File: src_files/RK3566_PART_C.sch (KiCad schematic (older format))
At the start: 1 part

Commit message: littleupdate
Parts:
- U1: renamed from U?; footprint (none) -> greencharge-footprints:BGA828C65P31X31_2100X2100X161N
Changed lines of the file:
@@
 $Descr A3 16535 11693
 encoding utf-8
-Sheet 8 11
+Sheet 10 11
 Title ""
 Date ""
@@
 P 7300 650
 AR Path="/61C7A3C9" Ref="U?"  Part="4"
-AR Path="/61C73AB6/61C7A3C9" Ref="U?"  Part="4"
-F 0 "U?" H 7325 315 50  0000 C CNN
+AR Path="/61C73AB6/61C7A3C9" Ref="U1"  Part="4"
+F 0 "U1" H 7325 315 50  0000 C CNN
 F 1 "RK3566" H 7325 224 50  0000 C CNN
-F 2 "" H 6750 550 50  0001 C CNN
+F 2 "greencharge-footprints:BGA828C65P31X31_2100X2100X161N" H 6750 550 50  0001 C CNN
 F 3 "" H 6750 550 50  0001 C CNN
 	4    7300 650

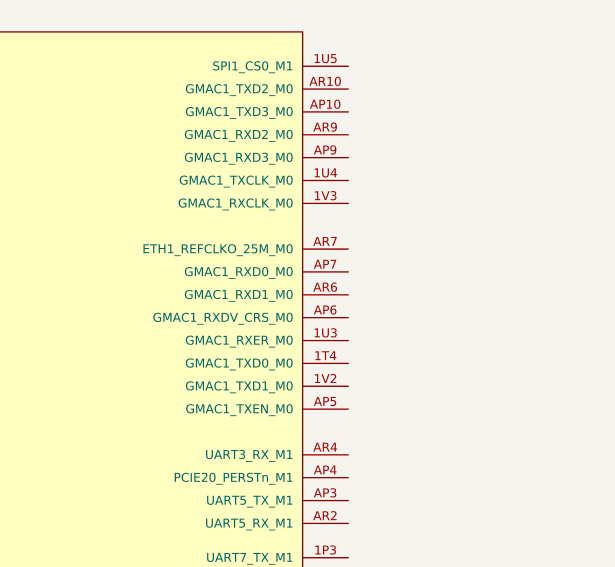
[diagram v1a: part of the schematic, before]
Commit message: gps add
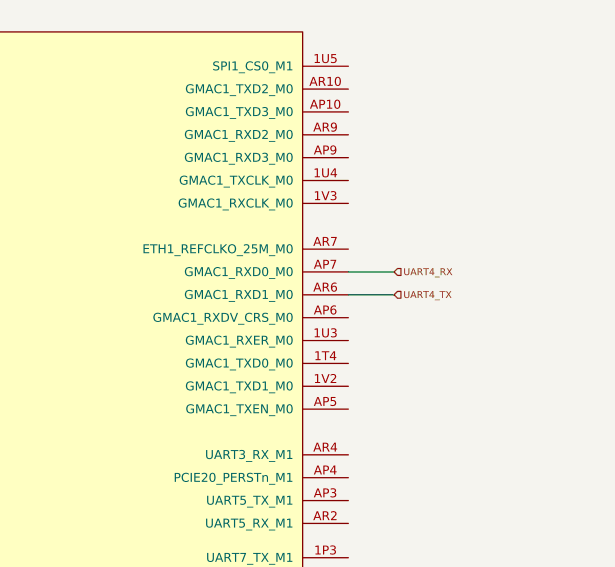
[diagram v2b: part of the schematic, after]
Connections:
- net UART4_RX: now reaches U1.AP7 (GMAC1_RXD0_M0)
- net UART4_TX: now reaches U1.AR6 (GMAC1_RXD1_M0)
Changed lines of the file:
@@
 Wire Wire Line
 	9475 5450 9350 5450
+Text HLabel 9550 2200 2    30   Input ~ 0
+UART4_RX
+Text HLabel 9550 2300 2    30   Input ~ 0
+UART4_TX
+Wire Wire Line
+	9550 2300 9350 2300
+Wire Wire Line
+	9550 2200 9350 2200
 $EndSCHEMATC

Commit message: added 3 screens
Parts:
- added C? (x12): 100nF, symbol Device:C_Small
- added C? (x5): 1uF, symbol Device:C_Small
- added C? (x4): 10uF, symbol Device:C_Small
- added J? (x2): 3-1734592-0, greencharge-footprints:TE_3-1734592-0, symbol 3-1734592-0:3-1734592-0
- added J?: 2001-1-2-21-00-BK, digikey-footprints:HDMI_Mini_Female_2001-1-2-21-00-BK, symbol dk_USB-DVI-HDMI-Connectors:2001-1-2-21-00-BK
- added R? (x4): 1R_1%, symbol Device:R_US
- added TP?: LVDS_TX0_AVDD_0V9, symbol Connector:TestPoint
- added TP?: LVDS_TX0_AVDD_1V8, symbol Connector:TestPoint
- added TP?: LVDS_TX1_AVDD_0V9, symbol Connector:TestPoint
- added TP?: LVDS_TX1_AVDD_1V8, symbol Connector:TestPoint
- added U? (x3): ESD5304D-TP, greencharge-footprints:ESD5304D-TP, symbol GCL_Integrated-Circuits:ESD5304D-TP
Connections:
- net 1N10: now reaches U1.1N10 (MIPI_DSI_TX1_AVDD_0V9)
- net 1N10: now also C?.1, R?.1, TP?.1
- net 1P11: now reaches U1.1P11 (MIPI_DSI_TX0/LVDS_TX0_AVDD_0V9)
- net 1P11: now also C?.1, R?.1, TP?.1
- net 1P12: now reaches U1.1P12 (MIPI_DSI_TX0/LVDS_TX0_AVDD_1V8)
- net 1P12: now also C?.1, R?.1, TP?.1
- net 1R10: now reaches U1.1R10 (IPI_DSI_TX1_AVDD_1V8)
- net 1R10: now also C?.1, R?.1, TP?.1
- net MIPI_DSI_TX1_CLKN-: now reaches U1.1U11 (MIPI_DSI_TX1_CLKn)
- net MIPI_DSI_TX1_CLKN-: now also J?.23
- net MIPI_DSI_TX1_CLKP+: now reaches U1.1V11 (MIPI_DSI_TX1_CLKp)
- net MIPI_DSI_TX1_CLKP+: now also J?.22
- net MIPI_DSI_TX0_CLKN-: now reaches U1.1V15 (MIPI_DSI_TX0_CLKn/LVDS_TX0_CLKn)
- net MIPI_DSI_TX0_CLKN-: now also J?.23
- net MIPI_DSI_TX0_CLKP+: now reaches U1.1V16 (MIPI_DSI_TX0_CLKp/LVDS_TX0_CLKp)
- net MIPI_DSI_TX0_CLKP+: now also J?.22
- net LCD_BL_PWM11_DISPLAY_ONE: now reaches U1.1V2 (GMAC1_TXD1_M0)
- net LCD_BL_PWM11_DISPLAY_ONE: now also J?.12
- net MIPI_DSI_TX1_D3N-: now reaches U1.AP20 (MIPI_DSI_TX1_D3n)
- net MIPI_DSI_TX1_D3N-: now also J?.29
- net MIPI_DSI_TX1_D2P+: now reaches U1.AP21 (MIPI_DSI_TX1_D2p)
- net MIPI_DSI_TX1_D2P+: now also J?.25
- net MIPI_DSI_TX1_D1N-: now reaches U1.AP23 (MIPI_DSI_TX1_D1n)
- net MIPI_DSI_TX1_D1N-: now also J?.20
- net MIPI_DSI_TX1_D0P+: now reaches U1.AP24 (MIPI_DSI_TX1_D0p)
- net MIPI_DSI_TX1_D0P+: now also J?.16
- net MIPI_DSI_TX0_D3N-: now reaches U1.AP26 (MIPI_DSI_TX0_D3n/LVDS_TX0_D3n)
- net MIPI_DSI_TX0_D3N-: now also J?.29
- net MIPI_DSI_TX0_D2P+: now reaches U1.AP27 (MIPI_DSI_TX0_D2p/LVDS_TX0_D2p)
- net MIPI_DSI_TX0_D2P+: now also J?.25
- net MIPI_DSI_TX0_D1N-: now reaches U1.AP29 (MIPI_DSI_TX0_D1n/LVDS_TX0_D1n)
- net MIPI_DSI_TX0_D1N-: now also J?.20
- net MIPI_DSI_TX0_D0P+: now reaches U1.AP30 (MIPI_DSI_TX0_D0p)
- net MIPI_DSI_TX0_D0P+: now also J?.16
- net HDMI_TX0N_PORT-: now reaches U1.AP33 (HDMI_TX_D0p)
- net HDMI_TX0N_PORT-: now also J?.9, U?.4
- net HDMI_TX1N_PORT-: now reaches U1.AP35 (HDMI_TX_D1n)
- net HDMI_TX1N_PORT-: now also J?.6, U?.1
- net HDMI_TX2P_PORT+: now reaches U1.AP36 (HDMI_TX_D2p)
- net HDMI_TX2P_PORT+: now also J?.1, U?.4
- net MIPI_DSI_TX1_D3P+: now reaches U1.AR20 (MIPI_DSI_TX1_D3p)
- net MIPI_DSI_TX1_D3P+: now also J?.28
- net MIPI_DSI_TX1_D2N-: now reaches U1.AR21 (MIPI_DSI_TX1_D2n)
- net MIPI_DSI_TX1_D2N-: now also J?.26
- net MIPI_DSI_TX1_D1P+: now reaches U1.AR23 (MIPI_DSI_TX1_D1p)
- net MIPI_DSI_TX1_D1P+: now also J?.19
- net MIPI_DSI_TX1_D0N-: now reaches U1.AR24 (MIPI_DSI_TX1_D0n)
- net MIPI_DSI_TX1_D0N-: now also J?.17
- net MIPI_DSI_TX0_D3P+: now reaches U1.AR26 (MIPI_DSI_TX0_D3p/LVDS_TX0_D3p)
- net MIPI_DSI_TX0_D3P+: now also J?.28
- net MIPI_DSI_TX0_D2N-: now reaches U1.AR27 (MIPI_DSI_TX0_D2n/LVDS_TX0_D2n)
- net MIPI_DSI_TX0_D2N-: now also J?.26
- net MIPI_DSI_TX0_D1P+: now reaches U1.AR29 (MIPI_DSI_TX0_D1p/LVDS_TX0_D1p)
- net MIPI_DSI_TX0_D1P+: now also J?.19
- net MIPI_DSI_TX0_D0N-: now reaches U1.AR30 (MIPI_DSI_TX0_D0n/LVDS_TX0_D0n)
- net MIPI_DSI_TX0_D0N-: now also J?.17
- net HDMI_TXCLKP_PORT+: now reaches U1.AR33 (HDMI_TX_D0n)
- net HDMI_TXCLKP_PORT+: now also J?.10, U?.3
- net HDMI_TX1P_PORT+: now reaches U1.AR35 (HDMI_TX_D1p)
- net HDMI_TX1P_PORT+: now also J?.4, U?.2
- net HDMI_TX2N_PORT-: now reaches U1.AR36 (HDMI_TX_D2n)
- net HDMI_TX2N_PORT-: now also J?.3, U?.3
- new net +5V: C?.1, C?.1, C?.1, C?.1, C?.1, C?.1, C?.1, C?.1, J?.1, J?.1, J?.2, J?.2, J?.3, J?.3
- new net BL_EN_GPIO0_C0: J?.11
- new net BL_EN_GPIO0_C0_DISPLAY_ONE: J?.11
- new net GND: C?.2, C?.2, C?.2, C?.2, C?.2, C?.2, C?.2, C?.2, C?.2, C?.2, C?.2, C?.2, C?.2, C?.2, C?.2, C?.2, C?.2, C?.2, C?.2, C?.2, C?.2, J?.11, J?.15, J?.15, J?.17, J?.18, J?.18, J?.2, J?.21, J?.21, J?.24, J?.24, J?.27, J?.27, J?.30, J?.30, J?.4, J?.4, J?.5, J?.8, J?.S1 (SHIELD), J?.S1 (SHIELD), J?.S2 (SHIELD), J?.S2 (SHIELD), U?.5 (GND), U?.5 (GND), U?.5 (GND)
- new net GNDPWR: J?.SH
- new net GPIO0_A0_DISPLAY_ONE: J?.5
- new net GPIO0_A0_DISPLAY_ZERO: J?.5
- new net HDMI_TX0P_PORT+: J?.7
- new net HDMI_TXCLKN_PORT-: J?.12, U?.2
- new net HDMI_TXDDC_SCL_PORT: J?.15, U?.4
- new net HDMI_TXDDC_SDA_PORT: J?.16, U?.3
- new net HDMI_TX_CEC_PORT: J?.13, U?.1
- new net HDMI_TX_HPD_PORT: J?.19, U?.2
- new net I2C2_SCL_M0_TP: J?.8, J?.8
- new net I2C2_SDA_M0_TP: J?.7, J?.7
- new net LCD_1_EN_GPIO0_C7: J?.9
- new net LCD_BL_PWM4: J?.12
- new net LCD_EN_GPIO0_C7: J?.9
- new net LCD_RST_L_GPIO0_C2: J?.13
- new net LCD_RST_L_GPIO0_C2_DISPLAY_ONE: J?.13
- new net TP_INT_GPIO0_A5: J?.10
- new net TP_INT_GPIO0_A5_DISPLAY_ONE: J?.10
- new net TP_RST_L_GPIO0_C5: J?.14
- new net TP_RST_L_GPIO0_C5_DISPLAY_ONE: J?.14
- new net VCC3V3_EXT: C?.1, C?.1, C?.1, C?.1, J?.6, J?.6
- new net VCC5V__HDMI_TX: C?.1, J?.18
- new net VCCA1V8_IMAGE: C?.1, C?.1, R?.2, R?.2
- new net VDDA0V9_IMAGE: C?.1, C?.1, R?.2, R?.2
- no-connect marks 1 -> 6
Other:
- note added: "DISPLAY_ZERO MIPI_TX(0)\nLCD/OLED CONN"
- note added: "ESD PROTECTION"
- note added: "HDMI CONNECTOR"
- note added: "MIPI_IMPEDANCE Z0=100ohm"
- moved on the sheet: U1D

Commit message: all screens added_3 items left
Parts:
- added C151, C152, C? (x2): 4.7uF, symbol Device:C_Small
- added C157, C158, C163, C? (x2): 100nF, symbol Device:C_Small
- added C?: 1uF, symbol Device:C_Small
- added D? (x3): 1N5819WS, Diode_SMD:D_SOD-323, symbol Device:D
- added D?: ESD5451R-2/TR, greencharge-footprints:DFP1006-2L, symbol Device:D_TVS
- added Q3, Q? (x2): Q_NMOS_GSD, symbol Device:Q_NMOS_GSD
- added R31, R32, R? (x2): 0R, symbol Device:R_US
- added R37, R38, R39, R40, R41, R42, R43, R44: 2.2R_5%, symbol Device:R_US
- added R45: 1.62K_1%, symbol Device:R_US
- added R46: 1K, symbol Device:R_US
- added R47: 100K, symbol Device:R_US
- added R?: 27K, symbol Device:R_US
- added R? (x2): 10K, symbol Device:R_US
- added R? (x2): 1.8K, symbol Device:R_US
- added TP1: HDMI_TX_AVDD_0V9, symbol Connector:TestPoint
- added TP2: HDMI_TX_AVDD_1V8, symbol Connector:TestPoint
- added TP?: EDP_TX_AVDD_0V9, symbol Connector:TestPoint
- added TP?: EDP_TX_AVDD_1V8, symbol Connector:TestPoint
- gave numbers to parts that had none: 35
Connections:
- net +5V: now also C?.1, D?.2 (A), D?.2 (A), D?.2 (A), Q3.1 (G)
- net GND: now also C151.2, C152.2, C157.2, C158.2, C163.2, C?.2, C?.2, C?.2, C?.2, C?.2, D?.2 (A2), R45.2, R47.2
- net HDMI_TX0N_PORT-: now also R42.2; no longer U1.AP33 (HDMI_TX_D0p)
- net HDMI_TX0P_PORT+: now also R41.2
- net HDMI_TX1N_PORT-: now also R40.2; no longer U1.AP35 (HDMI_TX_D1n)
- net HDMI_TX1P_PORT+: now also R38.2; no longer U1.AR35 (HDMI_TX_D1p)
- net HDMI_TX2N_PORT-: now also R39.2; no longer U1.AR36 (HDMI_TX_D2n)
- net HDMI_TX2P_PORT+: now also R37.2; no longer U1.AP36 (HDMI_TX_D2p)
- net HDMI_TXCLKN_PORT-: now also R44.2
- net HDMI_TXCLKP_PORT+: now also R43.2; no longer U1.AR33 (HDMI_TX_D0n)
- net HDMI_TXDDC_SCL_PORT: now also Q?.3 (D), R?.2
- net HDMI_TXDDC_SDA_PORT: now also Q?.3 (D), R?.2
- net HDMI_TX_CEC_PORT: now also Q3.3 (D)
- net HDMI_TX_HPD_PORT: now also R46.2, R47.1
- net VCCA1V8_IMAGE: now also C152.1, C?.1, R32.2, R?.2
- net VDDA0V9_IMAGE: now also C151.1, C?.1, R31.2, R?.2
- net 1G17: now reaches U1.1G17 (EDP_TX_AVDD_1V8)
- net 1G17: now also C?.1, R?.1, TP?.1
- net 1H17: now reaches U1.1H17 (EDP_TX_AVDD_0V9)
- net 1H17: now also C?.1, R?.1, TP?.1
- net EDP_TX_AUX+: now reaches U1.1H19 (EDP_TX_AUXp)
- net EDP_TX_AUXN-: now reaches U1.1H20 (EDP_TX_AUXn)
- net 1N14: now reaches U1.1N13 (HDMI_TX_AVDD_0V9_2)
- net 1N14: now also U1.1N14 (HDMI_TX_AVDD_0V9_1), C157.1, R31.1, TP1.1
- net 1P13: now reaches U1.1P13 (HDMI_TX_AVDD_1V8)
- net 1P13: now also C158.1, R32.1, TP2.1
- net at U1.1U16 (HDMI_TX_REXT): now also R45.1
- net MCDP_I2C_SDA: now reaches U1.1U3 (GMAC1_RXER_M0)
- net HDMI_TX_HPDIN: now reaches U1.1V17 (HDMI_TX_HPDIN)
- net HDMI_TX_HPDIN: now also C163.1, R46.1
- net at U1.AP32 (HDMI_TX_CLKn): now also R44.1
- net MCDP_I2C_SCL: now reaches U1.AP6 (GMAC1_RXDV_CRS_M0)
- net at U1.AR32 (HDMI_TX_CLKp): now also R43.1
- net EDP_TX_D0+: now reaches U1.J37 (EDP_TX_D0p)
- net EDP_TX_D0-: now reaches U1.J38 (EDP_TX_D0n)
- net EDP_TX_D1-: now reaches U1.K37 (EDP_TX_D1n)
- net EDP_TX_D1+: now reaches U1.K38 (EDP_TX_D1p)
- net EDP_TX_D2+: now reaches U1.M37 (EDP_TX_D2p)
- net EDP_TX_D2-: now reaches U1.M38 (EDP_TX_D2n)
- net VCC5V__HDMI_TX renamed VCC5V_HDMI_TX
- net VCC5V_HDMI_TX: now also D?.1 (A1), D?.1 (K)
- new net: R41.1, U1.AP33 (HDMI_TX_D0p)
- new net: R40.1, U1.AP35 (HDMI_TX_D1n)
- new net: R37.1, U1.AP36 (HDMI_TX_D2p)
- new net: R42.1, U1.AR33 (HDMI_TX_D0n)
- new net: R38.1, U1.AR35 (HDMI_TX_D1p)
- new net: R39.1, U1.AR36 (HDMI_TX_D2n)
- new net: D?.1 (K), R?.1 (x2)
- new net HDMITX_CEC_M0: Q3.2 (S), R?.2
- new net HDMITX_SCL: Q?.2 (S), R?.2
- new net HDMITX_SDA: Q?.2 (S), R?.2
- new net VCC_3V3: R?.1, R?.1, R?.1
- no-connect marks 6 -> 9
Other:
- note added: "DISPLAY PORT TO HDMI INTERFACE"
- note added: "HDMI SECTION"
- note added: "HDMI TX CEC"
- note added: "HDMI TX HPD"
- note added: "HDMI TX SCL\n"
- note added: "HDMI TX SDA"
- note added: "I2C5_SCL_M0 TO DP"
- note added: "I2C5_SDA_M0 TO DP"
- note added: "TO GPS MODULE"
- moved on the sheet: C153, C154, C155, C156, C159, C160, C161, C162, C164, C165, C166, C167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

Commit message: schematic capture complete
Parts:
- added C259: 100nF, Capacitor_SMD:C_0402_1005Metric, symbol Device:C_Small
- C151, C152, C153, C154, C155, C156, C157, C158, C159, C160, C161, C162, C163, C164, C165, C166, C167, C168, C169, C170, C171, C172, C173, C174, C175, C176: footprint (none) -> Capacitor_SMD:C_0402_1005Metric
- C186, C187, C188, C189, C190: renamed from C?; footprint (none) -> Capacitor_SMD:C_0402_1005Metric
- Q3: value Q_NMOS_GSD -> 2SK3018; footprint (none) -> digikey-footprints:SOT-23-3
- Q4, Q5: renamed from Q?; value Q_NMOS_GSD -> 2SK3018; footprint (none) -> digikey-footprints:SOT-23-3
- R31, R32, R33, R34, R35, R36, R37, R38, R39, R40, R41, R42, R43, R44, R45, R46, R47: footprint (none) -> Resistor_SMD:R_0402_1005Metric
- R58, R59, R60, R61, R62, R63, R64: renamed from R?; footprint (none) -> Resistor_SMD:R_0402_1005Metric
- TP1, TP2, TP3, TP4, TP5, TP6: footprint (none) -> TestPoint:TestPoint_Pad_D1.0mm
- TP7, TP8: renamed from TP?; footprint (none) -> TestPoint:TestPoint_Pad_D1.0mm
- gave numbers to parts that had none: 4
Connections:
- net GND: now also C259.2
- net VCC_3V3: now also Q4.1 (G), Q5.1 (G)
- net VCCIO_ACODEC: now reaches U1.1D13 (VCCIO1)
- net VCCIO_ACODEC: now also C259.1
- net I2C3_SCL_M1: now reaches U1.1T4 (GMAC1_TXD0_M0)
- net GPIO3_A3_d_TO_4G_MODEM_RESETn: now reaches U1.AP10 (GMAC1_TXD3_M0)
- net LCD_BL_PWM12_M0_DISPLAY_ONE: now reaches U1.AP5 (GMAC1_TXEN_M0)
- net LCD_BL_PWM12_M0_DISPLAY_ONE: now also J6.12
- net GPIO3_A2_d_TO_4G_MODEM_ON: now reaches U1.AR10 (GMAC1_TXD2_M0)
- net LCD_BL_PWM11_DISPLAY_ONE renamed I2C3_SDA_M1
- net I2C3_SDA_M1: no longer J6.12
- no-connect marks 9 -> 27
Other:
- moved on the sheet: C164, C166, C167, C170, C171, C174, J5

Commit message: updated footprint and schematics
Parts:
- removed J4: 2001-1-2-21-00-BK, digikey-footprints:HDMI_Mini_Female_2001-1-2-21-00-BK, symbol dk_USB-DVI-HDMI-Connectors:2001-1-2-21-00-BK
- added J4: 3-1734592-0, greencharge-footprints:TE_3-1734592-0, symbol 3-1734592-0:3-1734592-0
- U1: footprint greencharge-footprints:BGA828C65P31X31_2100X2100X161N -> greencharge-footprints:RK366_BGA-565_20x18_15.5x14.4mm
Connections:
- net labels added: AP_READY
- wire segments 385 -> 386
- no-connect marks 27 -> 26
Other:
- note added: "LINK FOR VIEW AND BUY: https://www.alibaba.com/product-detail/5-5-inch-HD-720-1080_62416915450.html"
- note added: "NOTE: SCREEN USED AS RECOMENDED IS A 4x AMOLED DISPLAY WITH 30 PIN MIPI FPC CONNECTION."
- note added: "change this to MIPI interface"
- moved on the sheet: C164, C166, C167, C170, C171, C174, J5
